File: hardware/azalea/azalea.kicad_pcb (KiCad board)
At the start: 4 copper layers, 70.6 x 53.3 mm, 88 parts, among them J1 NEIGHBOR1, J2 NEIGHBOR2, J3 USB-MICRO-B-SHIELDED, J4 USB-MICRO-B-SHIELDED, J5 JTAG, J7 BONUS_ROW, SW1 DFU, SW2 RESET, U1 LPC4330FBD144, U2 W25Q16DV, U3 AP7333, U4 IP4220CZ6, U5 NX5P2553GV, X1 XTAL4PIN, X2 RTC_XTAL

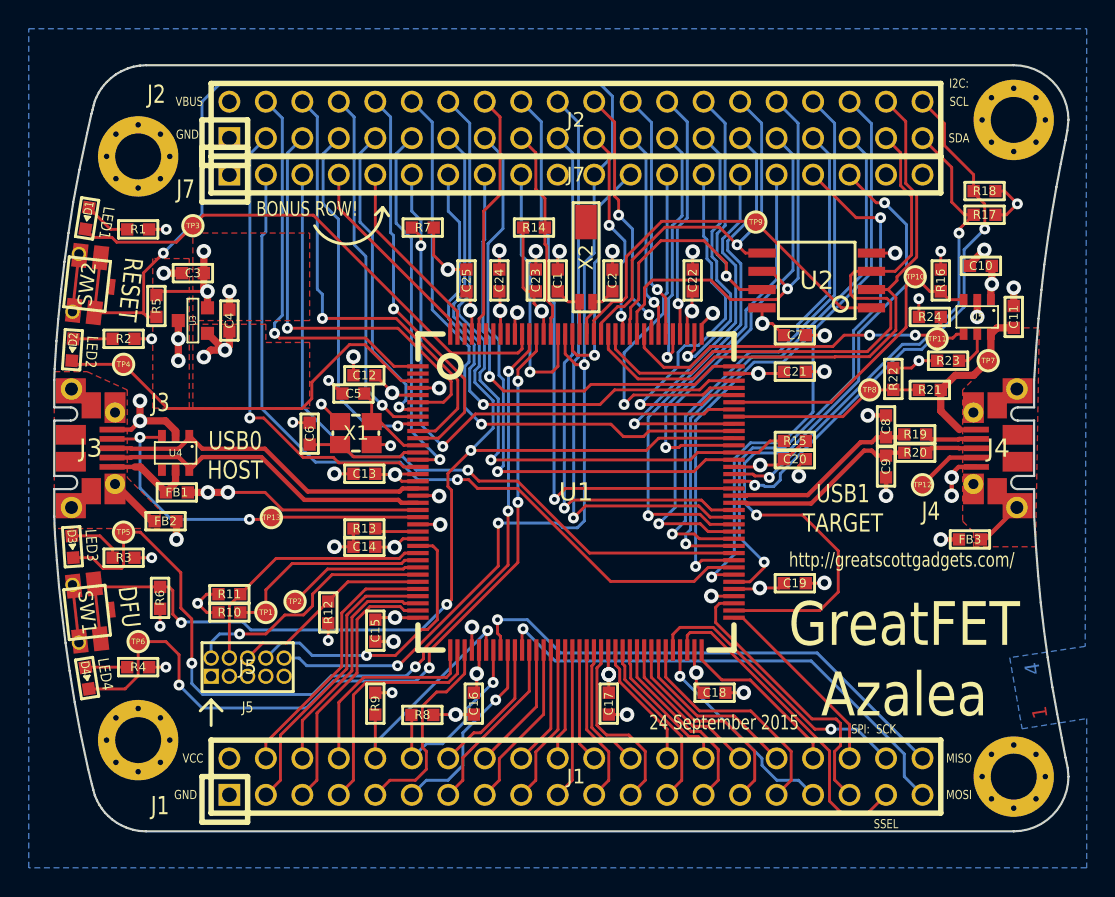
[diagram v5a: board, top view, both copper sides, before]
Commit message: fixed some 0603 modules that should have been 0805
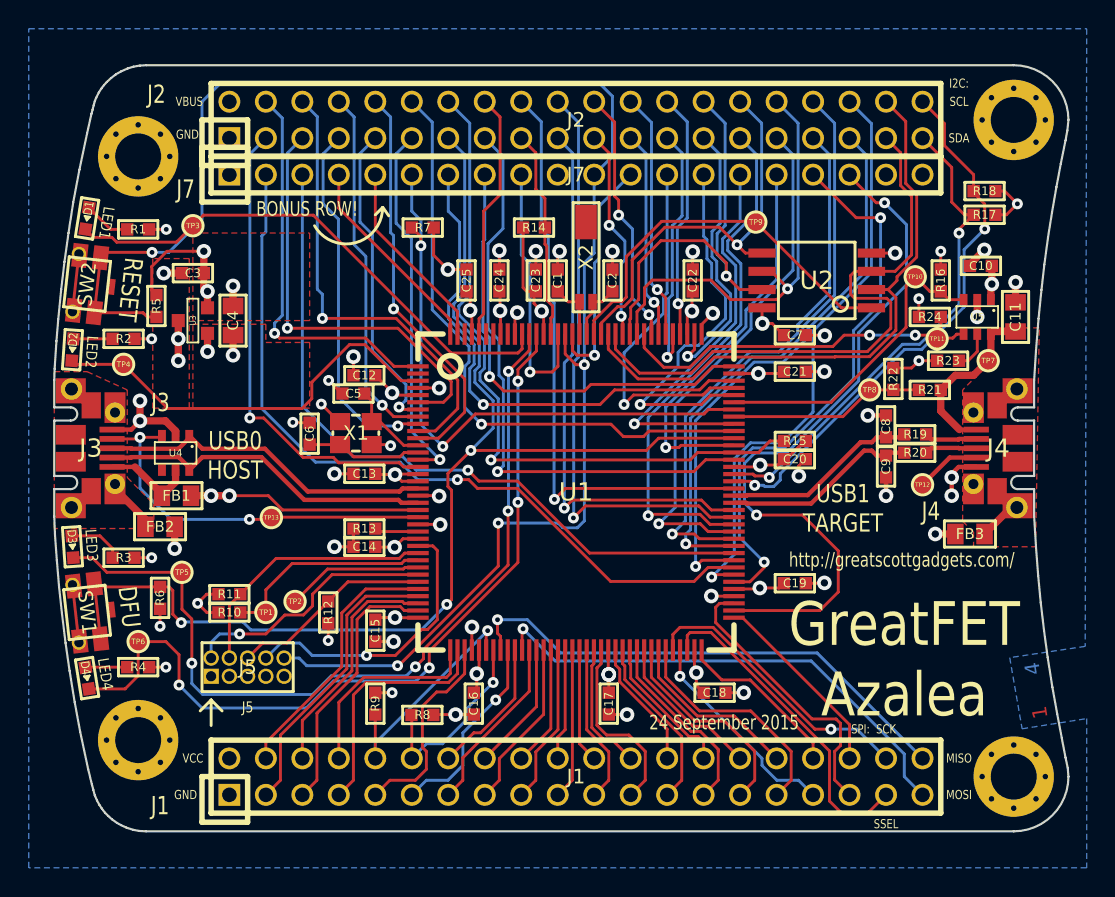
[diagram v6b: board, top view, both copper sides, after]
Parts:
- C11, C4, FB1, FB2, FB3: footprint gsg-modules:0603 -> gsg-modules:0805
- moved TP5 4.93 mm to (114.8, 106.4)
- moved FB2 0.54 mm to (113.3, 103.3)
- moved FB3 0.38 mm to (169.7, 103.8)
- moved C4 0.25 mm to (118.4, 88.9)
- moved FB1 0.23 mm to (114.4, 101.1)
- moved C11 0.13 mm to (172.8, 88.6)
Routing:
- net /LED3: track 62.6 -> 59.2 mm
- net VCC: track 84.9 -> 87.4 mm
- net /VBUS: track 23.7 -> 21.3 mm
- net GND: track 81.1 -> 81.7 mm

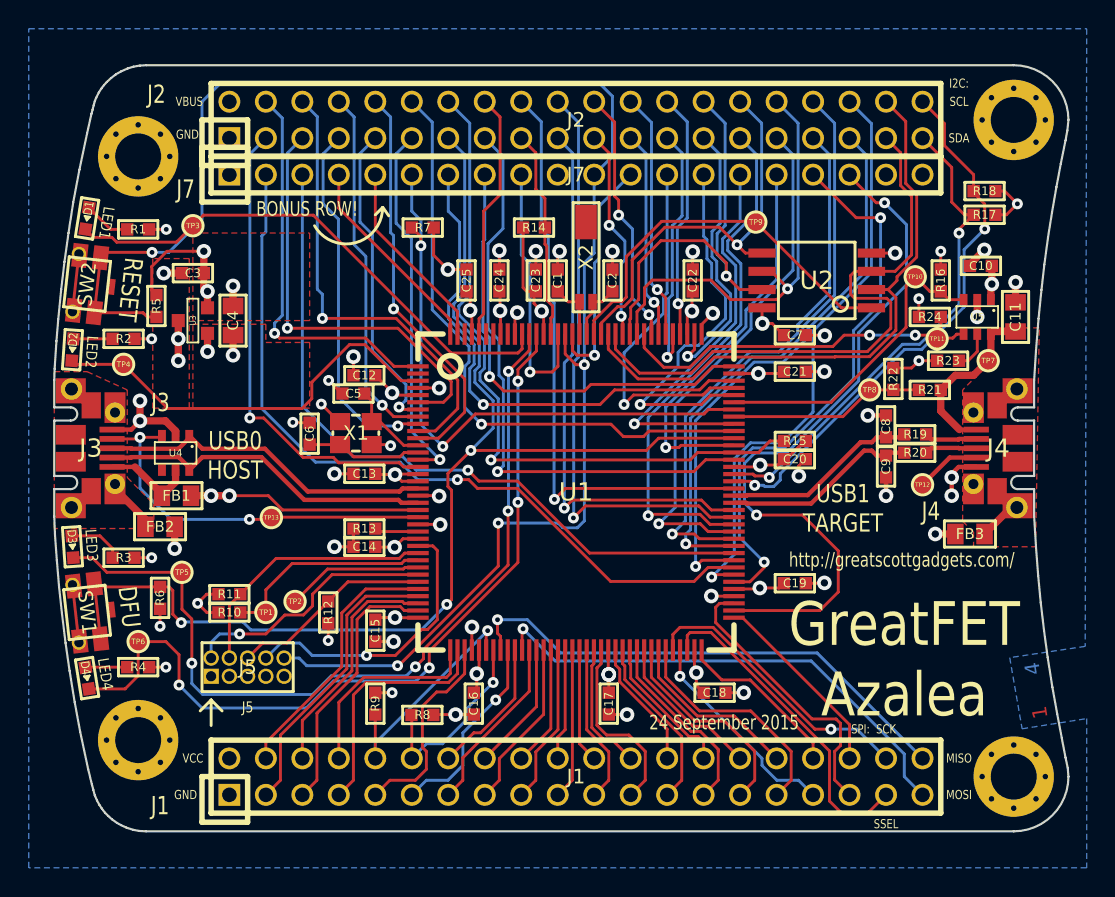
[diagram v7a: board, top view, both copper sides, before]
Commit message: azalea: made USB connectors protrude less from PCB edge, lengthened pads to ease soldering
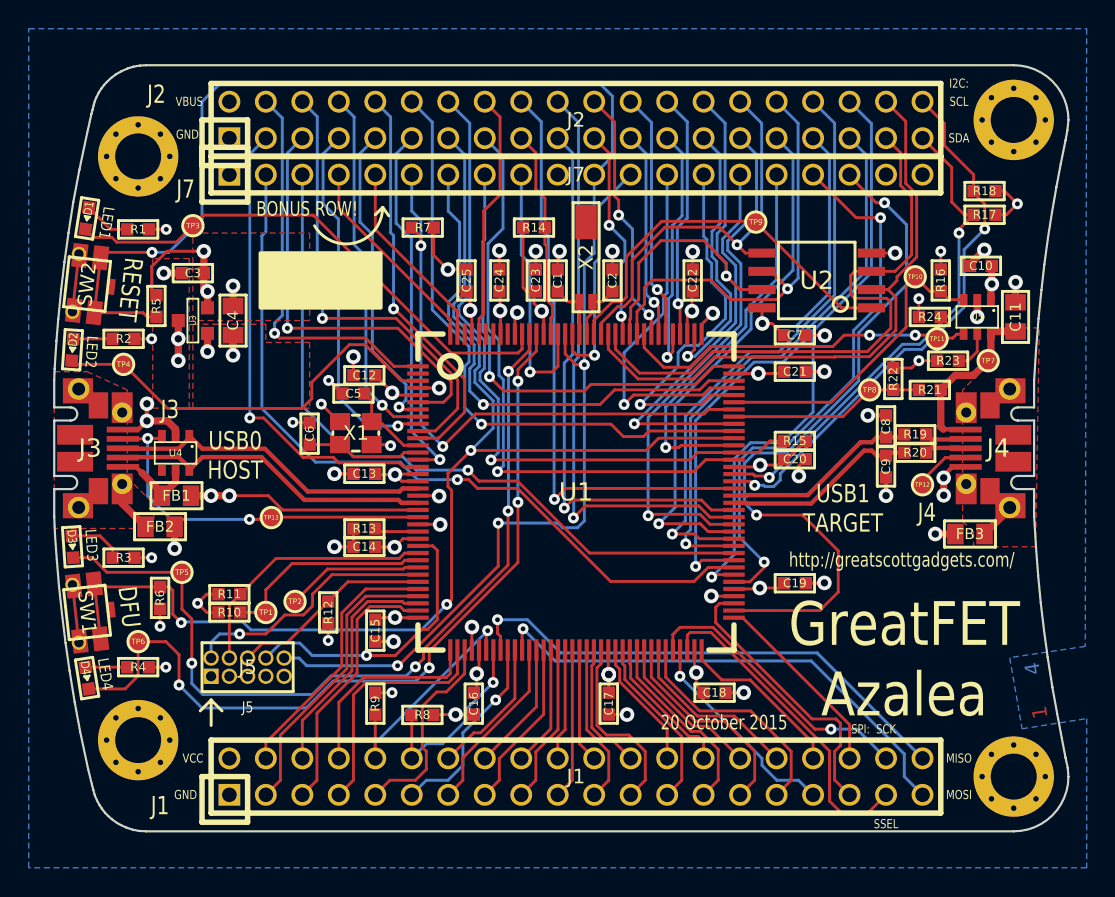
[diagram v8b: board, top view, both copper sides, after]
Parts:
- J3, J4: footprint gsg-modules:USB-MICROB-FCI-10103592-EXT -> gsg-modules:USB-MICROB-FCI-10103592-LONGPADS
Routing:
- net GND: track 81.7 -> 80.5 mm
- net /USB0_ID: track 27.4 -> 26.4 mm
- net Net-(FB1-Pad1): track 6.55 -> 5.84 mm
- net /USB1_ID: track 4.53 -> 3.96 mm
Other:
- board text added: "20 October 2015"
- board text removed: "24 September 2015"
